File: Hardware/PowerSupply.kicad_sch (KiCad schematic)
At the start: 26 parts

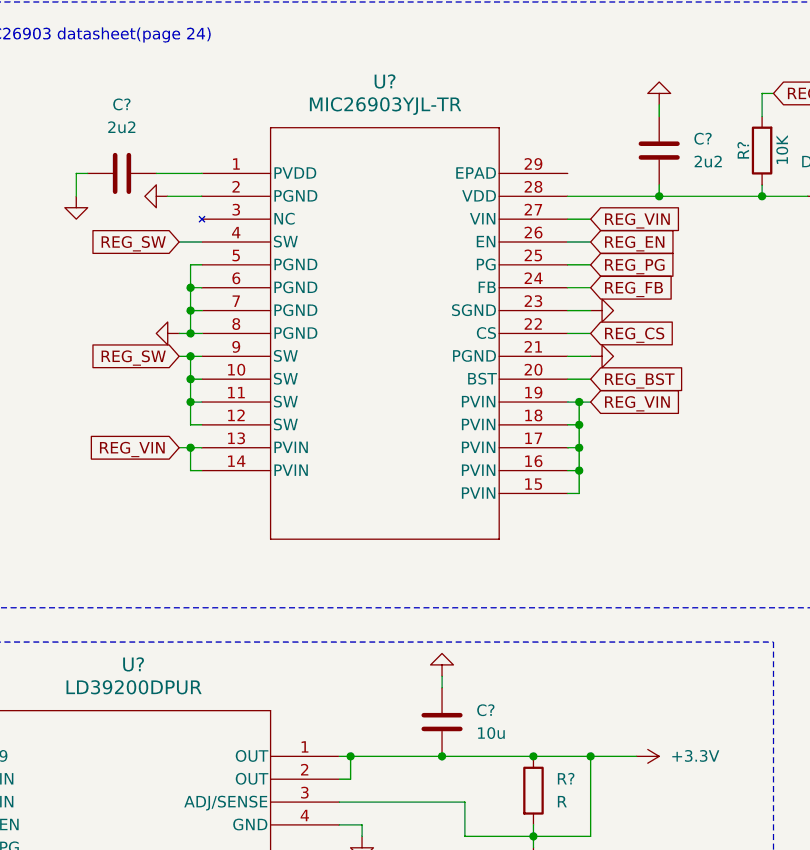
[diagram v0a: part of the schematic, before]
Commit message: added pdf schematic
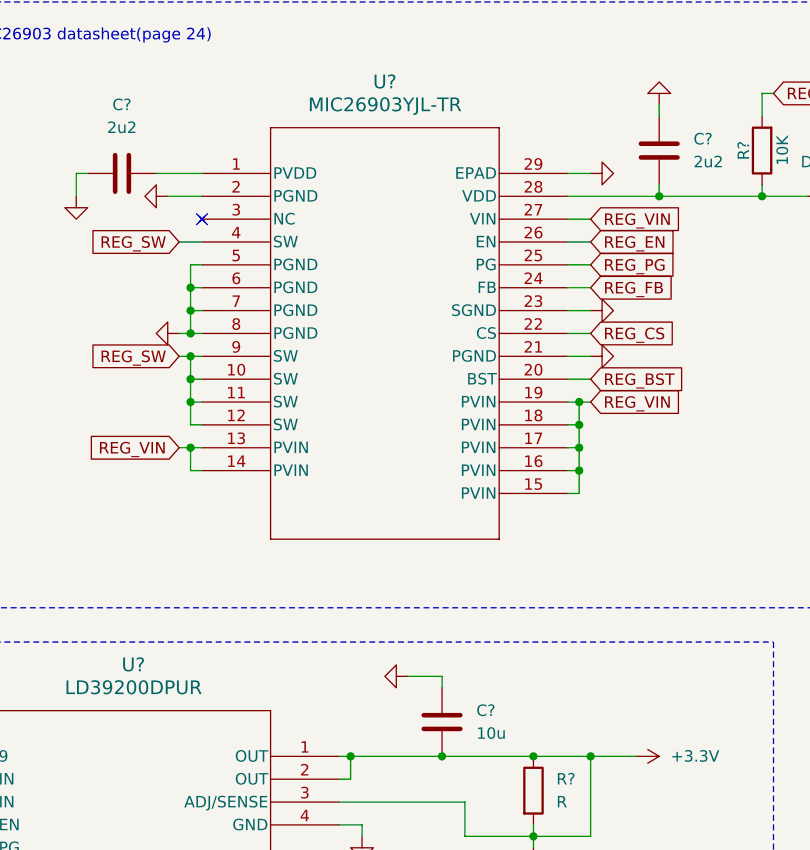
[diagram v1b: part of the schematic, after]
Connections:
- net GND: now also U?.29 (EPAD)
- no-connect marks 1 -> 2
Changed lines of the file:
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@@
 	)
 	(no_connect
+		(at 74.93 97.79)
+	)
+	(no_connect
 		(at 44.45 167.64)
 	)
@@
 	(wire
 		(pts
-			(xy 101.6 148.59) (xy 101.6 149.86)
+			(xy 115.57 92.71) (xy 118.11 92.71)
 		)
 		(stroke
@@
 	(wire
 		(pts
+			(xy 101.6 148.59) (xy 101.6 149.86)
+		)
+		(stroke
+			(width 0)
+			(type default)
+		)
+	)
+	(wire
+		(pts
 			(xy 115.57 110.49) (xy 118.11 110.49)
 		)
@@
 	(wire
 		(pts
+			(xy 97.79 148.59) (xy 101.6 148.59)
+		)
+		(stroke
+			(width 0)
+			(type default)
+		)
+	)
+	(wire
+		(pts
 			(xy 116.84 120.65) (xy 115.57 120.65)
 		)
@@
 	)
 	(symbol
+		(lib_id "power:GND")
+		(at 118.11 92.71 90)
+		(mirror x)
+		(unit 1)
+		(exclude_from_sim no)
+		(in_bom yes)
+		(on_board yes)
+		(dnp no)
+		(property "Reference" "#PWR023"
+			(at 124.46 92.71 0)
+			(effects
+				(font
+					(size 1.27 1.27)
+				)
+				(hide yes)
+			)
+		)
+		(property "Value" "GND"
+			(at 123.19 92.71 0)
+			(effects
+				(font
+					(size 1.27 1.27)
+				)
+				(hide yes)
+			)
+		)
+		(property "Footprint" ""
+			(at 118.11 92.71 0)
+			(effects
+				(font
+					(size 1.27 1.27)
+				)
+				(hide yes)
+			)
+		)
+		(property "Datasheet" ""
+			(at 118.11 92.71 0)
+			(effects
+				(font
+					(size 1.27 1.27)
+				)
+				(hide yes)
+			)
+		)
+		(property "Description" "Power symbol creates a global label with name \"GND\" , ground"
+			(at 118.11 92.71 0)
+			(effects
+				(font
+					(size 1.27 1.27)
+				)
+				(hide yes)
+			)
+		)
+		(pin "1"
+		)
+		(instances
+			(project "FCU"
+				(path "/f6ee1712-623f-481b-a021-3080378338dc/8abfa846-c73c-46a5-b4ec-bc41f97f15e7"
+					(reference "#PWR023")
+					(unit 1)
+				)
+			)
+		)
+	)
+	(symbol
 		(lib_id "Device:R")
 		(at 214.63 114.3 180)
@@
 	(symbol
 		(lib_id "power:GND")
-		(at 101.6 148.59 0)
+		(at 97.79 148.59 270)
 		(mirror x)
 		(unit 1)
@@
 		(dnp no)
 		(property "Reference" "#PWR020"
-			(at 101.6 142.24 0)
+			(at 91.44 148.59 0)
 			(effects
 				(font
@@
 		)
 		(property "Value" "GND"
-			(at 101.6 143.51 0)
+			(at 92.71 148.59 0)
 			(effects
 				(font
@@
 		)
 		(property "Footprint" ""
-			(at 101.6 148.59 0)
+			(at 97.79 148.59 0)
 			(effects
 				(font
@@
 		)
 		(property "Datasheet" ""
-			(at 101.6 148.59 0)
+			(at 97.79 148.59 0)
 			(effects
 				(font
@@
 		)
 		(property "Description" "Power symbol creates a global label with name \"GND\" , ground"
-			(at 101.6 148.59 0)
+			(at 97.79 148.59 0)
 			(effects
 				(font
